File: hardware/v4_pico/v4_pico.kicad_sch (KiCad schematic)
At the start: 107 parts, among them J1 joystick, J10 ON/OFF, J11 MIDI IN bk: 5 R: 4, J2 LED strip, J3 SSD1306 SPI, J4 MIDI OUT Y:M5 - R:M4, J5 Batt, J6 Neck - Y:O BK:B R:3.3, J7 01x03, J8 MXP5010, J9 Thumb, Q1 2N7000, SW1 SW_DIP_x01, U1 74HC165, U2 74HC165, U3 74HC165, U4 Pico, U5 FJ08K, U6 6N138, U7 MCP3002

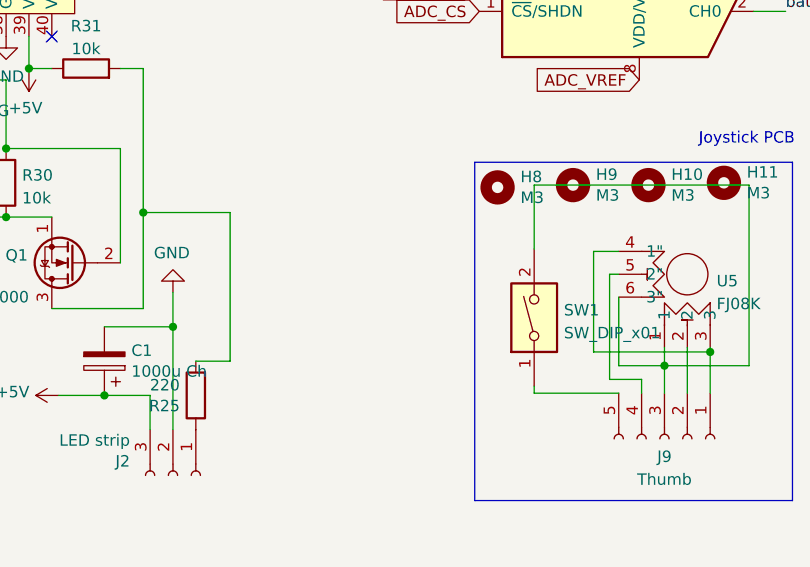
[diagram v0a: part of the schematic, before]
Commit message: Updated PCB with bite sensor
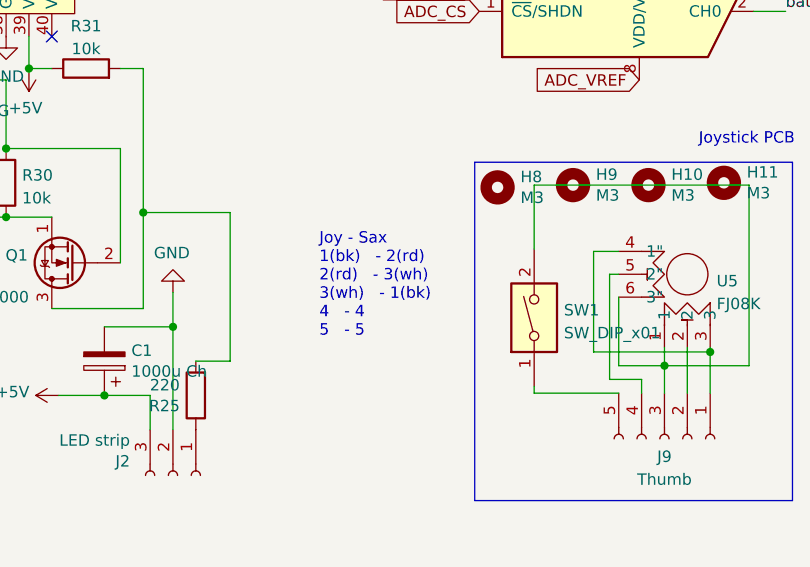
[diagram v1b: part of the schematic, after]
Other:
- note added: "Joy - Sax 1(bk) - 2(rd) 2(rd) - 3(wh) 3(wh) - 1(bk) 4 - 4 5 - 5"
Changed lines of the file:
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@@
+    (effects (font (size 1.27 1.27)) (justify left bottom))
+  )
+  (text "Joy - Sax\n1(bk)   - 2(rd)\n2(rd)   - 3(wh)\n3(wh)   - 1(bk)\n4   - 4\n5   - 5\n"
+    (at 197.358 142.24 0)
     (effects (font (size 1.27 1.27)) (justify left bottom))
   )
